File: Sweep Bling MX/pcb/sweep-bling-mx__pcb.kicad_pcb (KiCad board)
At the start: 2 copper layers, 113.5 x 95.2 mm, 31 parts, among them J2 AudioJack4dpb, SW10 SW_Push, SW11 SW_Push, SW12 SW_Push, SW14 SW_Push, SW15 SW_Push, SW16 SW_Push, SW17 SW_Push, SW18 SW_Push, SW2 SW_Push, SW20 SW_Push, SW21 SW_Push, SW3 SW_Push, SW4 SW_Push, SW5 SW_Push, SW6 SW_Push, SW8 SW_Push, SW9 SW_Push, U1 ProMicro-kbd

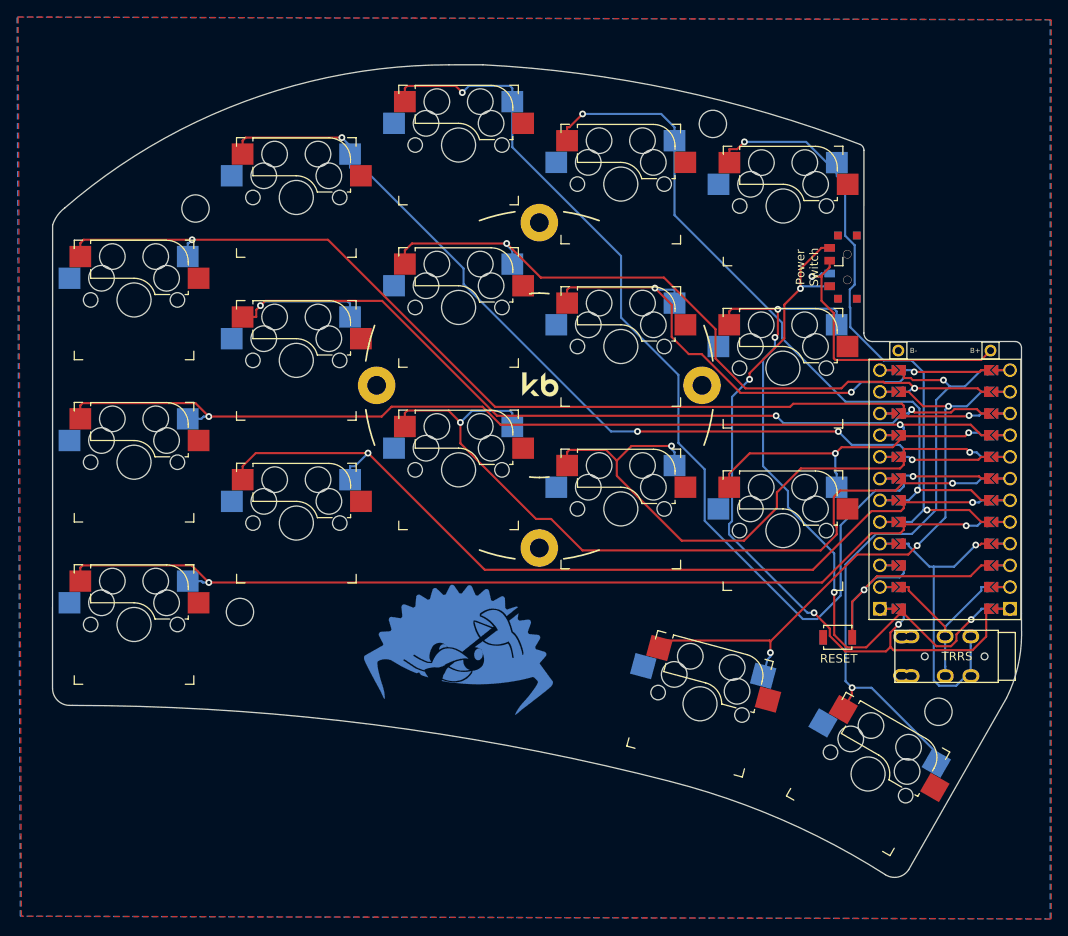
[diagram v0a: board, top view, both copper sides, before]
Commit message: Update silk and MCU orientation
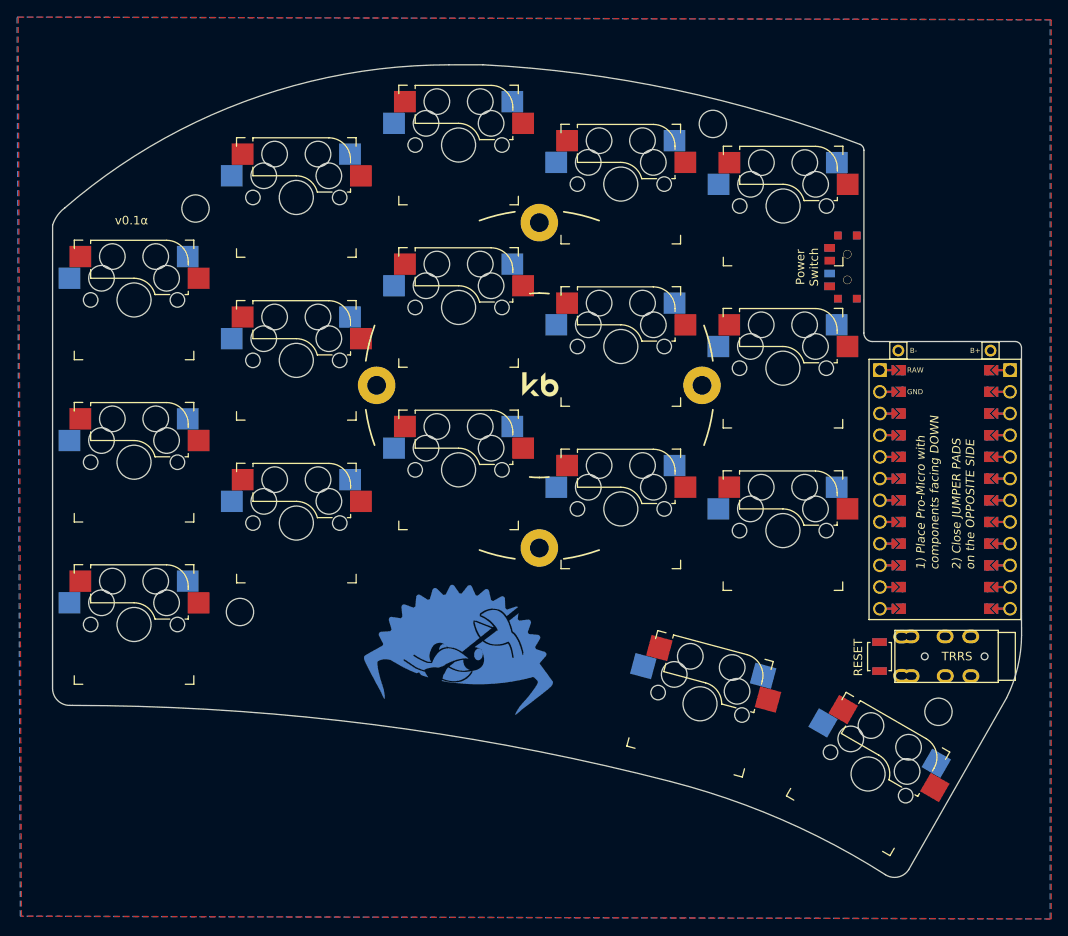
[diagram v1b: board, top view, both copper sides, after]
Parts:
- moved RST_B 5.39 mm to (132.3, 118.8), turned to 270 degrees
- moved RST_F 5.39 mm to (132.3, 118.8), turned to 270 degrees
- turned U1 to 270 degrees
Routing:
- net Switch3: track 125.4 -> 0.00 mm, vias 2 -> 0
- net Switch1: track 119.6 -> 0.00 mm, vias 2 -> 0
- net Switch11: track 114.9 -> 0.00 mm, vias 2 -> 0
- net Switch6: track 114.3 -> 0.00 mm, vias 2 -> 0
- net Switch7: track 107.9 -> 0.00 mm, vias 3 -> 0
- net Switch2: track 107.7 -> 0.00 mm, vias 4 -> 0
- net Switch12: track 103.3 -> 0.00 mm, vias 2 -> 0
- net Switch13: track 93.4 -> 0.00 mm, vias 2 -> 0
- net raw: track 88.2 -> 0.00 mm, vias 4 -> 0
- net Switch4: track 85.2 -> 0.00 mm, vias 2 -> 0
- net Switch8: track 84.0 -> 0.00 mm, vias 2 -> 0
- net Switch10: track 82.9 -> 0.00 mm, vias 4 -> 0
- net Switch5: track 74.3 -> 0.00 mm, vias 2 -> 0
- net Switch14: track 72.7 -> 0.00 mm, vias 2 -> 0
- net Switch17: track 72.0 -> 0.00 mm, vias 2 -> 0
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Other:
- board text added: "1) Place Pro-Micro with components facing DOWN"
- board text added: "2) Close JUMPER PADS on the OPPOSITE SIDE"
- board text added: "GND"
- board text added: "RAW"
- board text added: "v0.1α"

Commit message: Run auto router
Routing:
- net Switch1: track 0.00 -> 142.6 mm, vias 0 -> 2
- net Switch11: track 0.00 -> 125.3 mm, vias 0 -> 2
- net Switch6: track 0.00 -> 119.4 mm, vias 0 -> 2
- net Switch2: track 0.00 -> 118.7 mm, vias 0 -> 2
- net Switch7: track 0.00 -> 114.2 mm, vias 0 -> 3
- net Switch3: track 0.00 -> 104.4 mm, vias 0 -> 2
- net Switch8: track 0.00 -> 101.1 mm, vias 0 -> 3
- net Switch12: track 0.00 -> 97.6 mm, vias 0 -> 2
- net Switch4: track 0.00 -> 89.6 mm, vias 0 -> 2
- net Switch9: track 0.00 -> 82.6 mm, vias 0 -> 3
- net Switch5: track 0.00 -> 77.1 mm, vias 0 -> 2
- net Switch13: track 0.00 -> 75.9 mm, vias 0 -> 2
- net Switch16: track 0.00 -> 64.1 mm, vias 0 -> 1
- net Switch14: track 0.00 -> 57.9 mm, vias 0 -> 2
- net reset: track 0.00 -> 52.5 mm, vias 0 -> 2
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
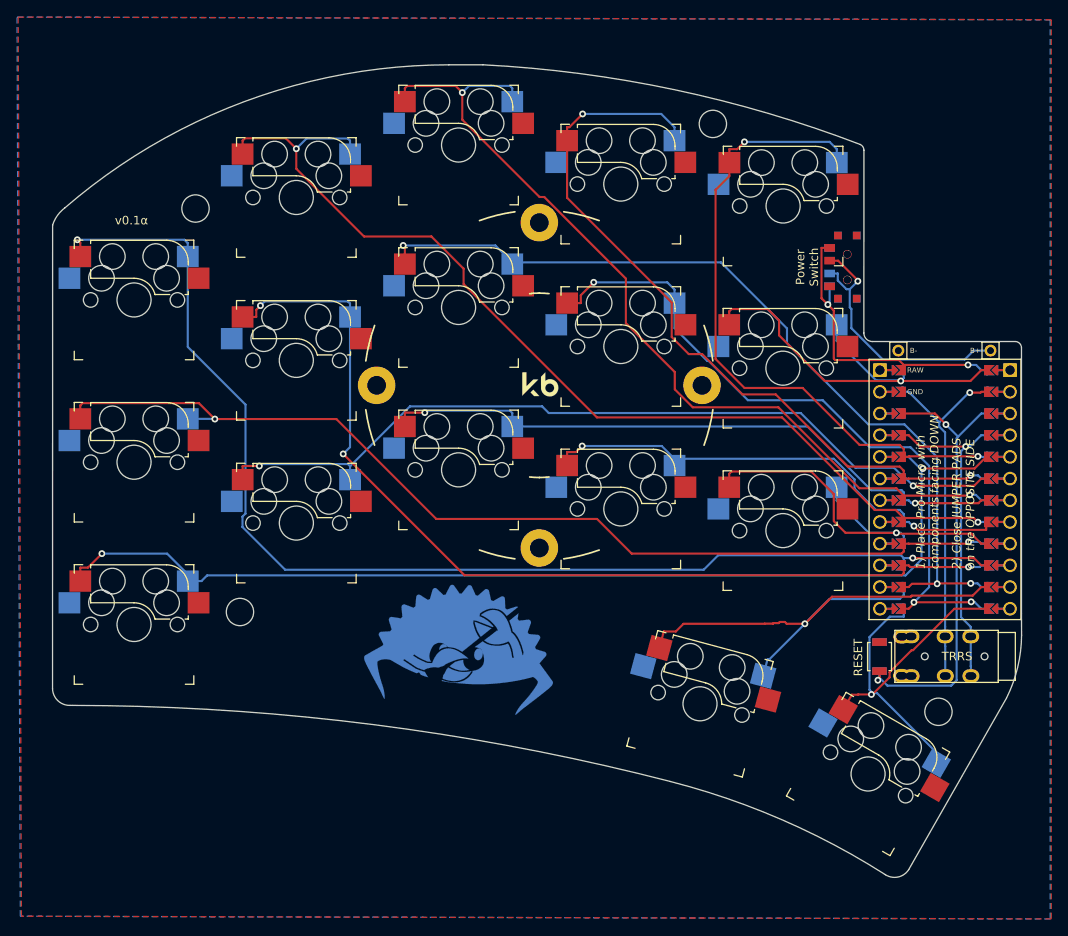
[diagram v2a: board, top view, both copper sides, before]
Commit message: Flip MCU pads for face down and re-route
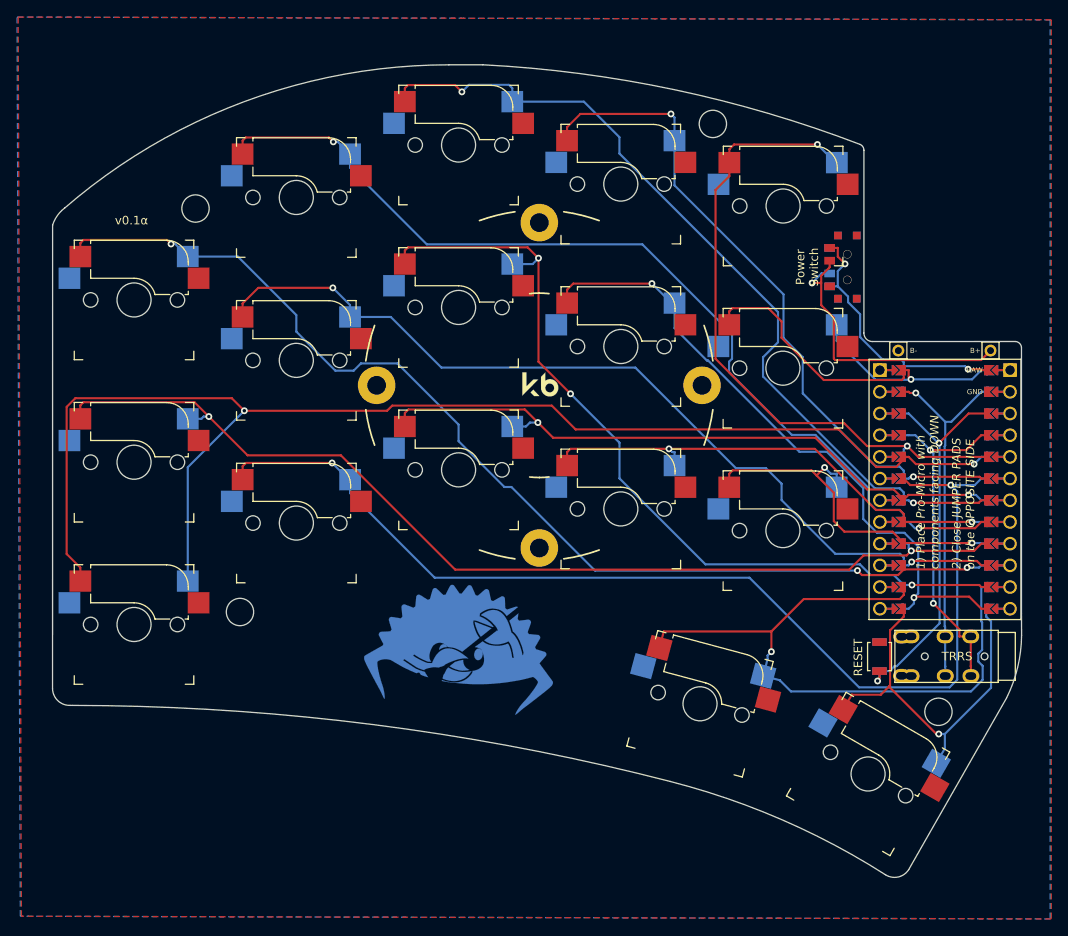
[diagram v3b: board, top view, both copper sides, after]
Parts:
- SW10, SW11, SW12, SW14, SW15, SW16, SW17, SW18, SW2, SW20, SW21, SW3, SW4, SW5, SW6, SW8, SW9: footprint Keyswitches by Daprice:Kailh_socket_MX_reversible_sameside -> Duckyb-Parts:Kailh_socket_MX_reversible_sameside_slot
- U1: footprint Promicro-Jumpers:ProMicro_unrouted -> Promicro-Jumpers:ProMicro_unrouted_facedown
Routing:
- net Switch12: track 97.6 -> 131.0 mm
- net Switch11: track 125.3 -> 157.2 mm
- net Switch1: track 142.6 -> 128.0 mm, vias 2 -> 3
- net Switch16: track 64.1 -> 77.0 mm
- net Switch4: track 89.6 -> 79.8 mm
- net Switch7: track 114.2 -> 105.8 mm, vias 3 -> 2
- net Switch15: track 49.2 -> 42.0 mm, vias 1 -> 2
- net reset: track 52.5 -> 45.5 mm
- net Switch9: track 82.6 -> 77.0 mm, vias 3 -> 2
- net Switch2: track 118.7 -> 113.6 mm
- net raw: track 35.8 -> 31.2 mm
- net Switch3: track 104.4 -> 100.3 mm
- net BT+_r: track 32.2 -> 35.0 mm
- net Switch13: track 75.9 -> 77.9 mm
- net vcc: track 38.3 -> 40.3 mm, vias 1 -> 2
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
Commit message: Add partial manual routing
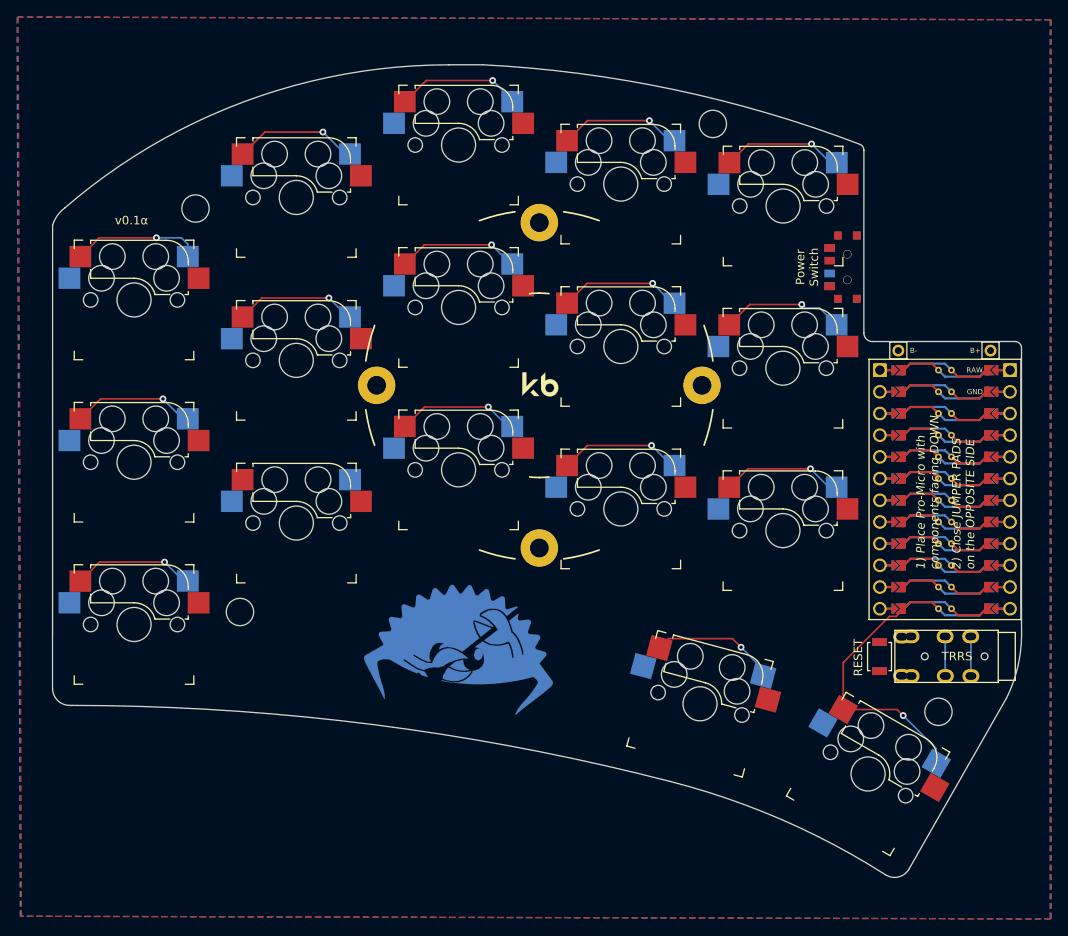
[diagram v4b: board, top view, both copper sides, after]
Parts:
- SW10, SW11, SW12, SW14, SW15, SW16, SW17, SW18, SW2, SW20, SW21, SW3, SW4, SW5, SW6, SW8, SW9: footprint Duckyb-Parts:Kailh_socket_MX_reversible_sameside_slot -> Keyswitches by Daprice:Kailh_socket_MX_reversible_sameside
- U1: footprint Promicro-Jumpers:ProMicro_unrouted_facedown -> Promicro-Jumpers:ProMicro_facedown
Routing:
- net Switch11: track 157.2 -> 14.4 mm, vias 2 -> 1
- net Switch12: track 131.0 -> 0.00 mm, vias 2 -> 0
- net Switch1: track 128.0 -> 15.2 mm, vias 3 -> 1
- net Switch6: track 121.3 -> 14.5 mm, vias 2 -> 1
- net Switch2: track 113.6 -> 14.7 mm, vias 2 -> 1
- net Switch7: track 105.8 -> 14.4 mm, vias 2 -> 1
- net Switch3: track 100.3 -> 14.7 mm, vias 2 -> 1
- net Switch8: track 99.4 -> 14.4 mm, vias 3 -> 1
- net Switch4: track 79.8 -> 14.5 mm, vias 2 -> 1
- net Switch13: track 77.9 -> 14.5 mm, vias 2 -> 1
- net Switch9: track 77.0 -> 14.5 mm, vias 2 -> 1
- net Switch5: track 76.8 -> 14.4 mm, vias 2 -> 1
- net Switch16: track 77.0 -> 14.8 mm
- net reset: track 45.5 -> 0.00 mm, vias 2 -> 0
- net Switch14: track 57.3 -> 14.5 mm, vias 2 -> 1
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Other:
- net class Default: trace_width 0.25 -> 0.2

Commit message: Finish manual routing
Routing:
- net Switch6: track 14.5 -> 153.5 mm
- net Switch1: track 15.2 -> 132.9 mm, vias 1 -> 3
- net Switch7: track 14.4 -> 124.5 mm
- net Switch11: track 14.4 -> 119.7 mm
- net Switch2: track 14.7 -> 113.7 mm
- net Switch12: track 0.00 -> 93.8 mm, vias 0 -> 1
- net Switch8: track 14.4 -> 103.4 mm
- net Switch3: track 14.7 -> 99.6 mm
- net Switch4: track 14.5 -> 86.0 mm
- net Switch5: track 14.4 -> 84.0 mm
- net vcc: track 4.64 -> 74.2 mm, vias 0 -> 6
- net Switch9: track 14.5 -> 83.7 mm
- net Switch13: track 14.5 -> 70.9 mm
- net reset: track 0.00 -> 55.1 mm, vias 0 -> 4
- net Switch18: track 4.64 -> 58.1 mm, vias 0 -> 3
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
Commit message: Fix DRC issues
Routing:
- net reset: track 55.1 -> 58.7 mm, vias 4 -> 5
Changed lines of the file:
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@@
     (thickness 1.6)
     (drawings 34)
-    (tracks 460)
+    (tracks 467)
     (zones 0)
     (modules 31)
@@
   (segment (start 118.6815 105.918) (end 119.539097 105.918) (width 0.2) (layer B.Cu) (net 2))
   (segment (start 119.539097 105.918) (end 127.295246 113.674149) (width 0.2) (layer B.Cu) (net 2))
-  (segment (start 141.79 121.034) (end 142.99 121.034) (width 0.2) (layer F.Cu) (net 2))
-  (segment (start 140.68999 122.13401) (end 141.79 121.034) (width 0.2) (layer F.Cu) (net 2))
-  (segment (start 132.127008 122.13401) (end 140.68999 122.13401) (width 0.2) (layer F.Cu) (net 2))
-  (segment (start 129.58449 119.591492) (end 132.127008 122.13401) (width 0.2) (layer F.Cu) (net 2))
-  (segment (start 129.58449 115.963393) (end 129.58449 119.591492) (width 0.2) (layer F.Cu) (net 2))
-  (segment (start 127.295246 113.674149) (end 129.58449 115.963393) (width 0.2) (layer F.Cu) (net 2))
   (segment (start 126.827808 91.403925) (end 126.495012 91.071129) (width 0.2) (layer B.Cu) (net 2))
   (segment (start 125.107129 91.071129) (end 125.095 91.059) (width 0.2) (layer F.Cu) (net 2))
@@
   (via (at 125.095 91.059) (size 0.8) (drill 0.4) (layers F.Cu B.Cu) (net 2))
   (via (at 126.495012 91.071129) (size 0.8) (drill 0.4) (layers F.Cu B.Cu) (net 2))
+  (segment (start 141.79 121.034) (end 142.99 121.034) (width 0.2) (layer F.Cu) (net 2))
+  (segment (start 140.142 122.682) (end 141.79 121.034) (width 0.2) (layer F.Cu) (net 2))
+  (segment (start 132.674998 122.682) (end 140.142 122.682) (width 0.2) (layer F.Cu) (net 2))
+  (segment (start 129.58449 119.591492) (end 132.674998 122.682) (width 0.2) (layer F.Cu) (net 2))
+  (segment (start 127.295246 113.674149) (end 129.58449 115.963393) (width 0.2) (layer F.Cu) (net 2))
+  (segment (start 129.58449 115.963393) (end 129.58449 119.591492) (width 0.2) (layer F.Cu) (net 2))
   (segment (start 139.99 116.424) (end 139.97 116.404) (width 0.2) (layer B.Cu) (net 3))
   (segment (start 139.99 121.034) (end 139.99 116.424) (width 0.2) (layer B.Cu) (net 3))
@@
   (segment (start 121.8565 94.08796) (end 121.456501 94.487959) (width 0.2) (layer F.Cu) (net 4))
   (segment (start 121.456501 94.487959) (end 121.456501 101.171015) (width 0.2) (layer F.Cu) (net 4))
+  (via (at 133.1595 121.92) (size 0.8) (drill 0.4) (layers F.Cu B.Cu) (net 4))
+  (segment (start 132.291 120.458) (end 132.291 121.0515) (width 0.2) (layer F.Cu) (net 4))
+  (segment (start 132.291 121.0515) (end 133.1595 121.92) (width 0.2) (layer F.Cu) (net 4))
+  (segment (start 133.1595 121.92) (end 132.759501 121.520001) (width 0.2) (layer B.Cu) (net 4))
+  (segment (start 132.289 121.108) (end 132.289 120.458) (width 0.2) (layer B.Cu) (net 4))
+  (segment (start 132.701001 121.520001) (end 132.289 121.108) (width 0.2) (layer B.Cu) (net 4))
+  (segment (start 132.759501 121.520001) (end 132.701001 121.520001) (width 0.2) (layer B.Cu) (net 4))
   (via (at 47.625 69.723) (size 0.8) (drill 0.4) (layers F.Cu B.Cu) (net 5))
   (segment (start 40.932 69.723) (end 47.625 69.723) (width 0.2) (layer F.Cu) (net 5))
